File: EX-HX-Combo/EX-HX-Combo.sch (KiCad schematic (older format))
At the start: 34 parts, among them CN1 DB9 Male, J1 IDE_CONNECTOR, J2 Jumpers, J3 Bus_Tandy_Plus, U1 BIOS FLASH, U2 74HCT245, U3 1.8432 MHz, U4 DS1315, U5 AS6C4008-55PCN, U6 16550/16C550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

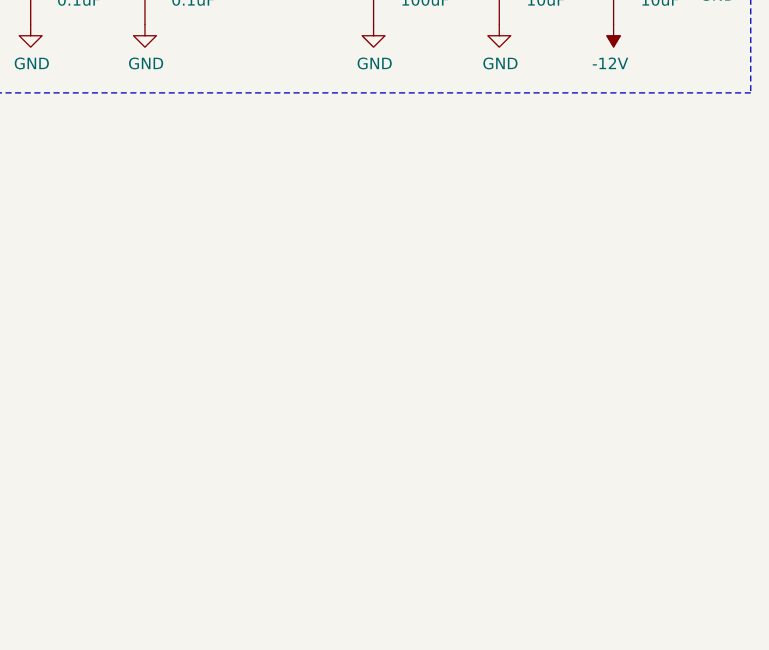
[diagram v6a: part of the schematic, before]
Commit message: Add mounting holes to EX-HX-Combo schematic.
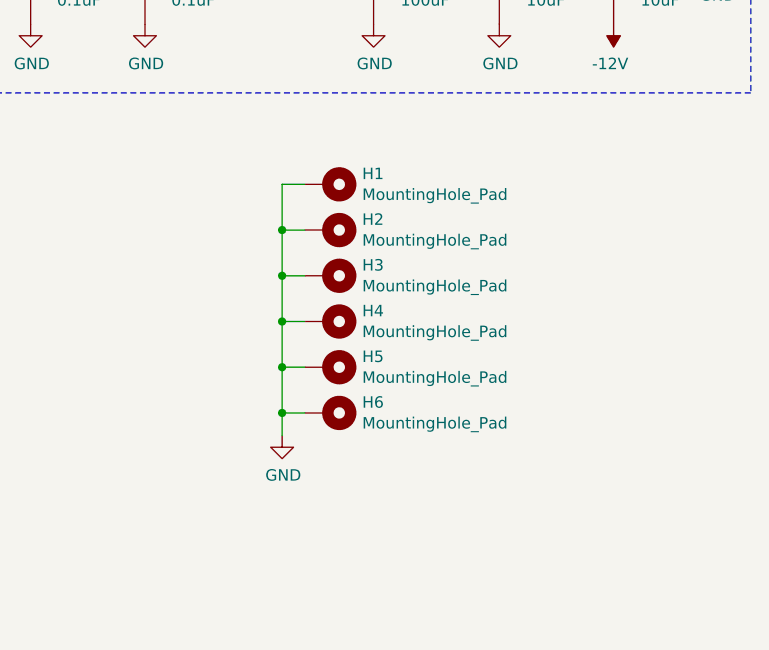
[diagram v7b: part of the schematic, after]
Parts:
- added H1, H2, H3, H4, H5, H6: MountingHole_Pad, MountingHole:MountingHole_3.5mm_Pad, symbol Mechanical:MountingHole_Pad
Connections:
- net GND: now also H1.1, H2.1, H3.1, H4.1, H5.1, H6.1
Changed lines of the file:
@@
 	1    0    0    -1
 $EndComp
+$Comp
+L Mechanical:MountingHole_Pad H1
+U 1 1 60D6980C
+P 13200 8550
+F 0 "H1" V 13154 8700 50  0000 L CNN
+F 1 "MountingHole_Pad" V 13245 8700 50  0000 L CNN
+F 2 "MountingHole:MountingHole_3.5mm_Pad" H 13200 8550 50  0001 C CNN
+F 3 "~" H 13200 8550 50  0001 C CNN
+	1    13200 8550
+	0    1    1    0
+$EndComp
+$Comp
+L Mechanical:MountingHole_Pad H2
+U 1 1 60D6AC46
+P 13200 8750
+F 0 "H2" V 13154 8900 50  0000 L CNN
+F 1 "MountingHole_Pad" V 13245 8900 50  0000 L CNN
+F 2 "MountingHole:MountingHole_3.5mm_Pad" H 13200 8750 50  0001 C CNN
+F 3 "~" H 13200 8750 50  0001 C CNN
+	1    13200 8750
+	0    1    1    0
+$EndComp
+$Comp
+L Mechanical:MountingHole_Pad H3
+U 1 1 60D6B05B
+P 13200 8950
+F 0 "H3" V 13154 9100 50  0000 L CNN
+F 1 "MountingHole_Pad" V 13245 9100 50  0000 L CNN
+F 2 "MountingHole:MountingHole_3.5mm_Pad" H 13200 8950 50  0001 C CNN
+F 3 "~" H 13200 8950 50  0001 C CNN
+	1    13200 8950
+	0    1    1    0
+$EndComp
+$Comp
+L Mechanical:MountingHole_Pad H4
+U 1 1 60D6B294
+P 13200 9150
+F 0 "H4" V 13154 9300 50  0000 L CNN
+F 1 "MountingHole_Pad" V 13245 9300 50  0000 L CNN
+F 2 "MountingHole:MountingHole_3.5mm_Pad" H 13200 9150 50  0001 C CNN
+F 3 "~" H 13200 9150 50  0001 C CNN
+	1    13200 9150
+	0    1    1    0
+$EndComp
+$Comp
+L Mechanical:MountingHole_Pad H5
+U 1 1 60D6B4F1
+P 13200 9350
+F 0 "H5" V 13154 9500 50  0000 L CNN
+F 1 "MountingHole_Pad" V 13245 9500 50  0000 L CNN
+F 2 "MountingHole:MountingHole_3.5mm_Pad" H 13200 9350 50  0001 C CNN
+F 3 "~" H 13200 9350 50  0001 C CNN
+	1    13200 9350
+	0    1    1    0
+$EndComp
+Wire Wire Line
+	13100 8550 13000 8550
+Wire Wire Line
+	13000 8550 13000 8750
+Wire Wire Line
+	13100 9350 13000 9350
+Connection ~ 13000 9350
+Wire Wire Line
+	13000 9350 13000 9550
+Wire Wire Line
+	13000 9150 13100 9150
+Connection ~ 13000 9150
+Wire Wire Line
+	13000 9150 13000 9350
+$Comp
+L Mechanical:MountingHole_Pad H6
+U 1 1 60D9AE58
+P 13200 9550
+F 0 "H6" V 13154 9700 50  0000 L CNN
+F 1 "MountingHole_Pad" V 13245 9700 50  0000 L CNN
+F 2 "MountingHole:MountingHole_3.5mm_Pad" H 13200 9550 50  0001 C CNN
+F 3 "~" H 13200 9550 50  0001 C CNN
+	1    13200 9550
+	0    1    1    0
+$EndComp
+Wire Wire Line
+	13100 9550 13000 9550
+Connection ~ 13000 9550
+Wire Wire Line
+	13000 9550 13000 9650
+$Comp
+L power:GND #PWR0148
+U 1 1 60DA739E
+P 13000 9650
+F 0 "#PWR0148" H 13000 9400 50  0001 C CNN
+F 1 "GND" H 13005 9477 50  0000 C CNN
+F 2 "" H 13000 9650 50  0001 C CNN
+F 3 "" H 13000 9650 50  0001 C CNN
+	1    13000 9650
+	1    0    0    -1
+$EndComp
+Wire Wire Line
+	13100 8950 13000 8950
+Connection ~ 13000 8950
+Wire Wire Line
+	13000 8950 13000 9150
+Wire Wire Line
+	13100 8750 13000 8750
+Connection ~ 13000 8750
+Wire Wire Line
+	13000 8750 13000 8950
 $EndSCHEMATC

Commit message: Initial experimentation with component placement in EX-HX-Combo.
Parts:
- U2: footprint Package_SO:SOIC-20W_7.5x12.8mm_P1.27mm -> Package_DIP:DIP-20_W7.62mm_Socket
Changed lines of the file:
@@
 F 0 "U2" H 10800 2950 50  0000 C CNN
 F 1 "74HCT245" H 10800 2850 50  0000 C CNN
-F 2 "Package_SO:SOIC-20W_7.5x12.8mm_P1.27mm" H 10600 2200 50  0001 C CNN
+F 2 "Package_DIP:DIP-20_W7.62mm_Socket" H 10600 2200 50  0001 C CNN
 F 3 "http://www.ti.com/lit/gpn/sn74LS245" H 10600 2200 50  0001 C CNN
 	1    10600 2200
